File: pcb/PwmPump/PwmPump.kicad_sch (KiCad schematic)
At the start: 7 parts, among them J1 3.5mm, J2 3.5mm, SW1 RotaryEncoder_Switch, U1 WEMOS_C3_mini, U2 BOB-12009

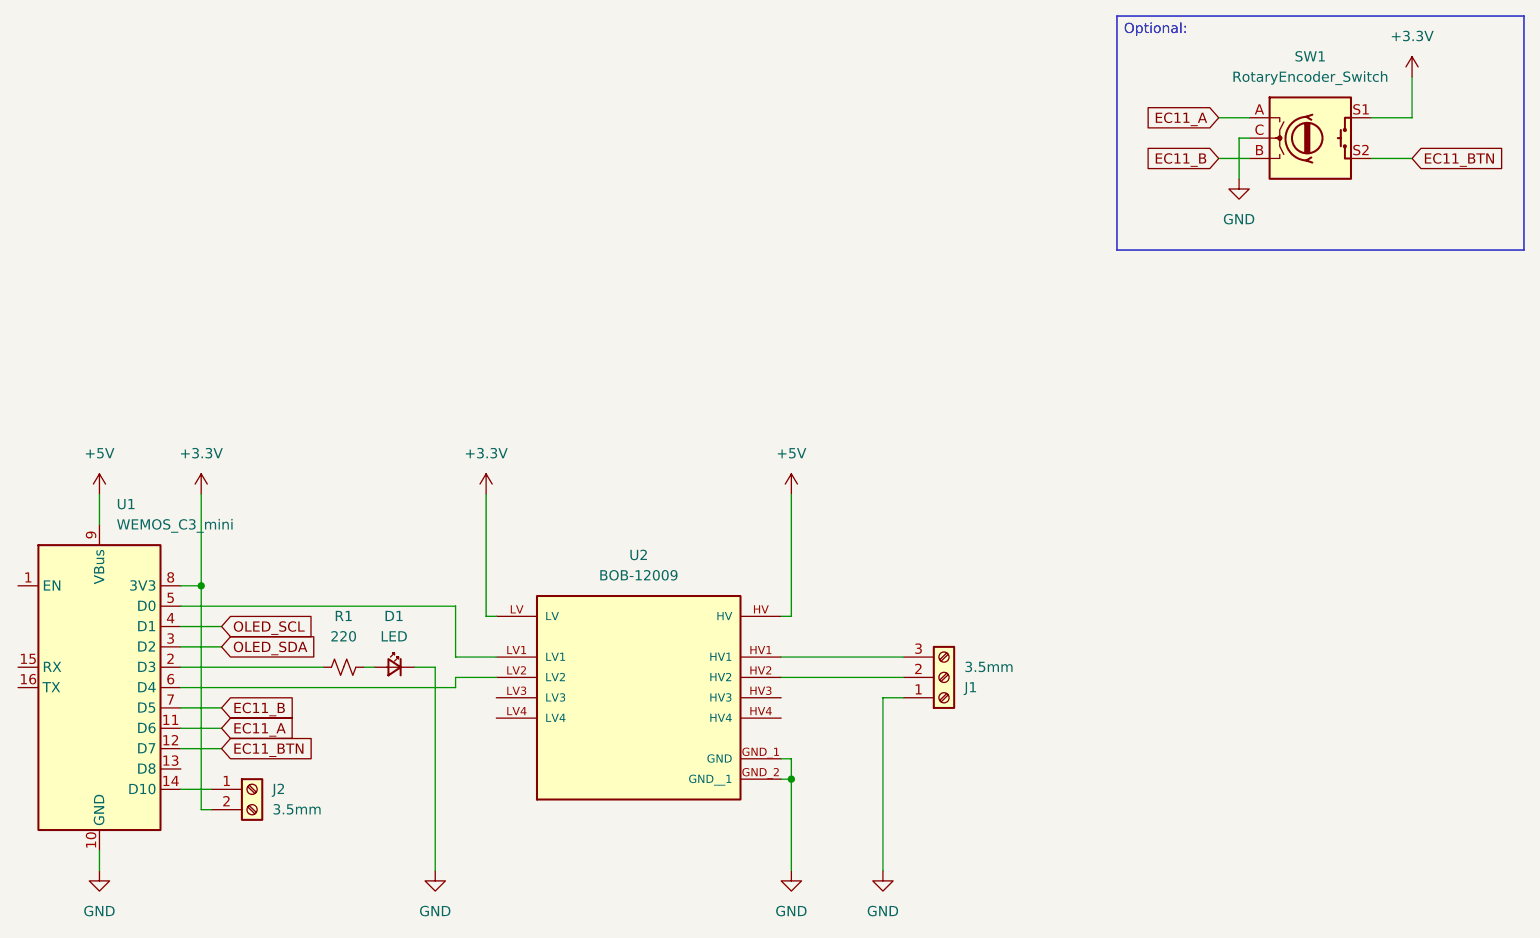
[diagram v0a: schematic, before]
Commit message: Updated: Added 2nd analog input
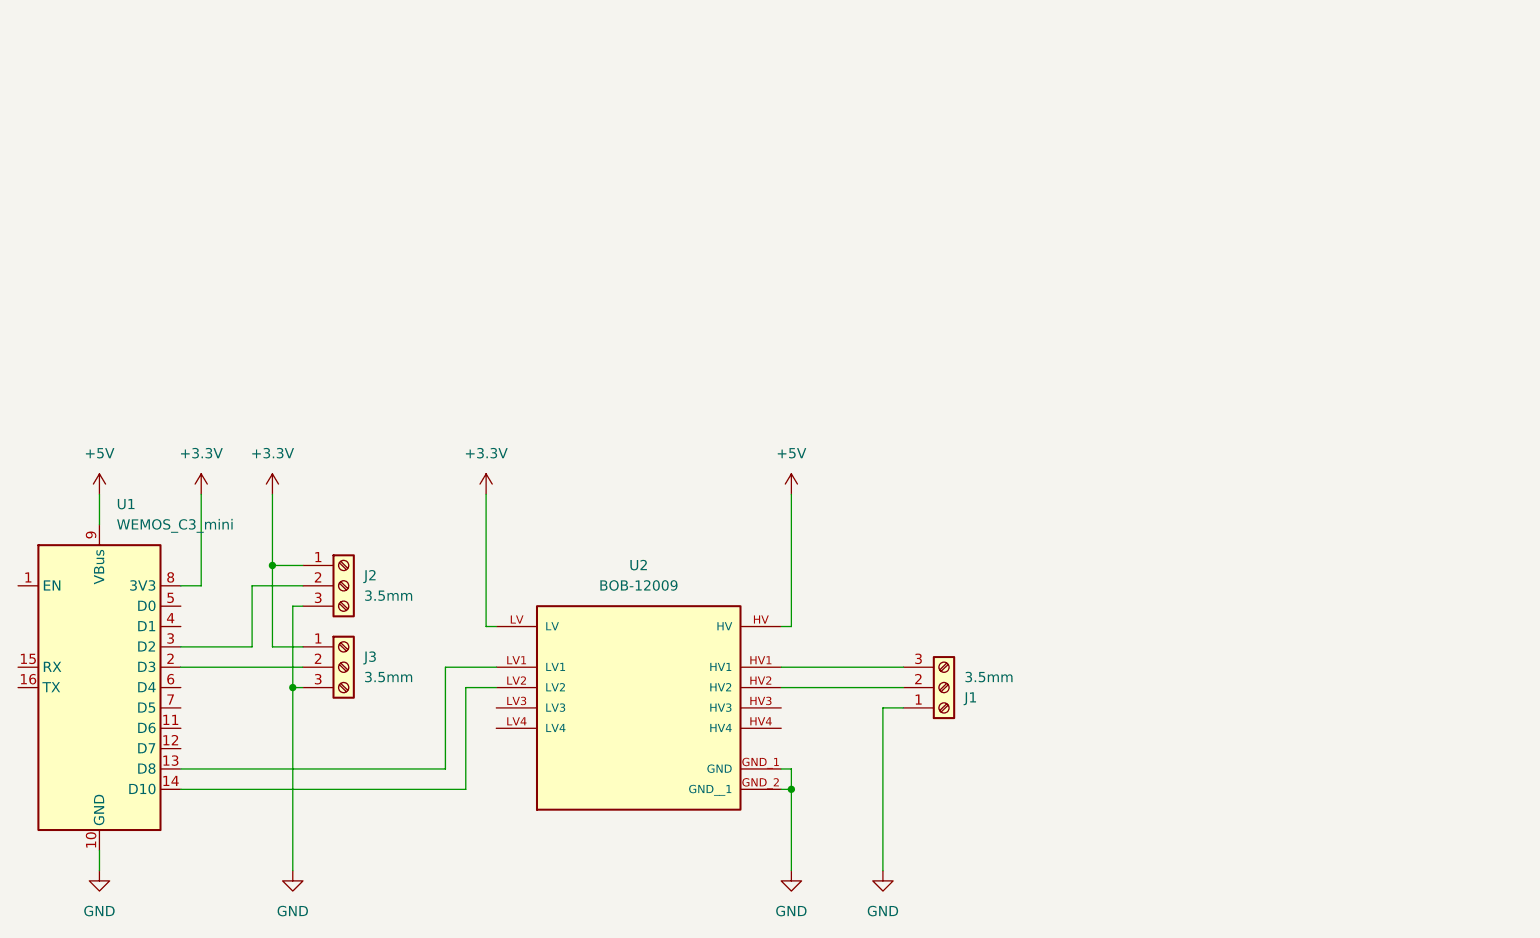
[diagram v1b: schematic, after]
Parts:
- removed D1: LED, LED_THT:LED_D3.0mm, symbol PCM_SparkFun-LED:LED
- removed R1: 220, Resistor_THT:R_Axial_DIN0207_L6.3mm_D2.5mm_P10.16mm_Horizontal, symbol PCM_SparkFun-Resistor:220_0402
- removed SW1: RotaryEncoder_Switch, symbol Device:RotaryEncoder_Switch
- added J3: 3.5mm, PCM_SparkFun-Connector:ScrewTerminal_1x03_P3.5mm_Horizontal_Black, symbol PCM_SparkFun-Connector:ScrewTerminal_1x03_P3.5mm_Horizontal_Black
- J2: footprint PCM_SparkFun-Connector:ScrewTerminal_1x02_P3.5mm_Horizontal_Black -> PCM_SparkFun-Connector:ScrewTerminal_1x03_P3.5mm_Horizontal_Black; symbol PCM_SparkFun-Connector:ScrewTerminal_1x02_P3.5mm_Horizontal_Black -> PCM_SparkFun-Connector:ScrewTerminal_1x03_P3.5mm_Horizontal_Black; PROD_ID CONN-08399 -> CONN-08288
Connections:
- net +3.3V: now also J2.1 (Pin_1), J3.1 (Pin_1); no longer J2.2 (Pin_2)
- net GND: now also J2.3 (Pin_3), J3.3 (Pin_3)
- net at U2.LV1: now also U1.13 (D8); no longer U1.5 (D0)
- net at U2.LV2: now also U1.14 (D10); no longer U1.6 (D4)
- net at U1.2 (D3): now also J3.2 (Pin_2)
- net EC11_A: no longer names the net of U1.11 (D6)
- net EC11_B: no longer names the net of U1.7 (D5)
- net EC11_BTN: no longer names the net of U1.12 (D7)
- net OLED_SCL: no longer names the net of U1.4 (D1)
- net OLED_SDA: no longer names the net of U1.3 (D2)
- net OLED_SDA: now also J2.2 (Pin_2)
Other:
- note removed: "Optional:"
- moved on the sheet: J1, U2
